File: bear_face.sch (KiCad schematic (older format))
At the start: 277 parts, among them J1 USB_B_Micro, J2 Conn_02x03_Odd_Even, Q1 2N7002, SW1 SW_Push, U1 ATmega32U4-AU, U2 SRV05-4, Y1 16MHz

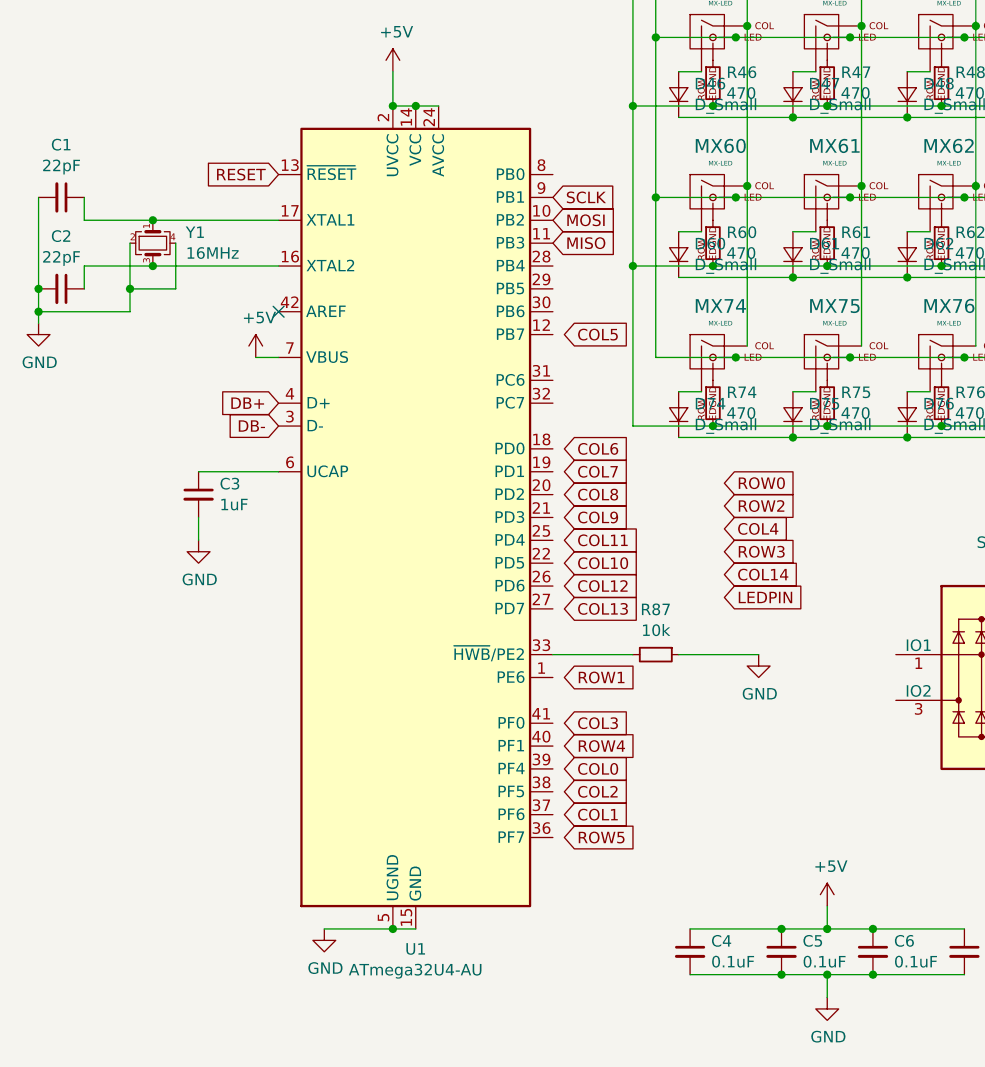
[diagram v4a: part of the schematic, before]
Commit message: +5V net tied in, matrix started
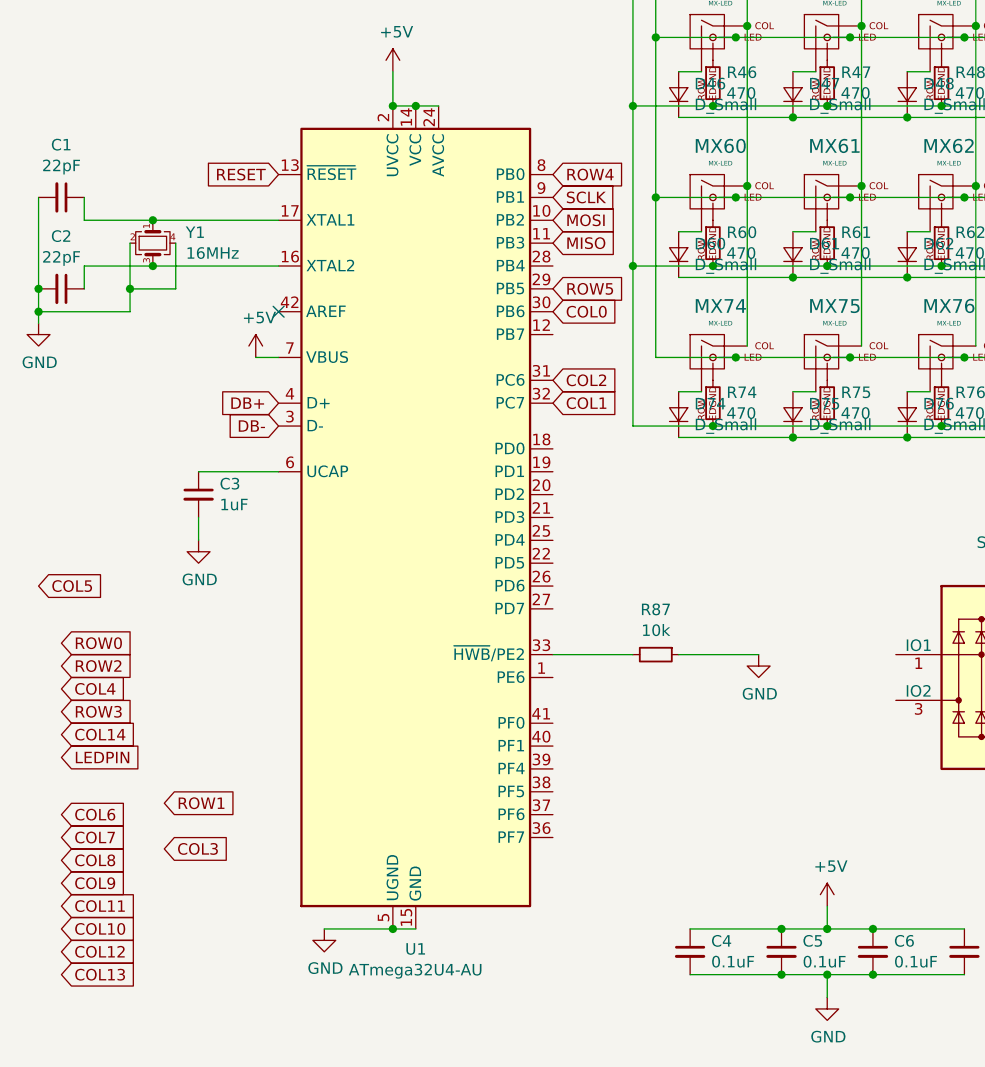
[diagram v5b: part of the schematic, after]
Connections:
- net COL0: now also U1.30 (PB6)
- net COL1: now also U1.32 (PC7)
- net COL2: now also U1.31 (PC6)
- net ROW4: now also U1.8 (PB0)
- net ROW5: now also U1.29 (PB5)
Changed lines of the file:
@@
 	1    0    0    -1
 $EndComp
-Text GLabel 3050 6700 2    50   Input ~ 0
+Text GLabel 3000 4300 2    50   Input ~ 0
 ROW5
-Text GLabel 3050 6200 2    50   Input ~ 0
+Text GLabel 1300 6750 2    50   Input ~ 0
 COL3
 NoConn ~ 1800 4400
-Text GLabel 3750 5150 2    50   Input ~ 0
+Text GLabel 850  5850 2    50   Input ~ 0
 ROW0
-Text GLabel 3050 6000 2    50   Input ~ 0
+Text GLabel 1300 6550 2    50   Input ~ 0
 ROW1
-Text GLabel 3750 5250 2    50   Input ~ 0
+Text GLabel 850  5950 2    50   Input ~ 0
 ROW2
-Text GLabel 3750 5450 2    50   Input ~ 0
+Text GLabel 850  6150 2    50   Input ~ 0
 ROW3
-Text GLabel 3050 4500 2    50   Input ~ 0
+Text GLabel 750  5600 2    50   Input ~ 0
 COL5
-Text GLabel 3050 5100 2    50   Input ~ 0
+Text GLabel 850  6700 2    50   Input ~ 0
 COL7
-Text GLabel 3050 5200 2    50   Input ~ 0
+Text GLabel 850  6800 2    50   Input ~ 0
 COL8
-Text GLabel 3050 5300 2    50   Input ~ 0
+Text GLabel 850  6900 2    50   Input ~ 0
 COL9
-Text GLabel 3050 5500 2    50   Input ~ 0
+Text GLabel 850  7100 2    50   Input ~ 0
 COL10
-Text GLabel 3050 5400 2    50   Input ~ 0
+Text GLabel 850  7000 2    50   Input ~ 0
 COL11
-Text GLabel 3050 5600 2    50   Input ~ 0
+Text GLabel 850  7200 2    50   Input ~ 0
 COL12
-Text GLabel 3050 5700 2    50   Input ~ 0
+Text GLabel 850  7300 2    50   Input ~ 0
 COL13
-Text GLabel 3750 5550 2    50   Input ~ 0
+Text GLabel 850  6250 2    50   Input ~ 0
 COL14
-Text GLabel 3750 5350 2    50   Input ~ 0
+Text GLabel 850  6050 2    50   Input ~ 0
 COL4
-Text GLabel 3050 5000 2    50   Input ~ 0
+Text GLabel 850  6600 2    50   Input ~ 0
 COL6
-Text GLabel 3050 6300 2    50   Input ~ 0
+Text GLabel 3000 3800 2    50   Input ~ 0
 ROW4
 Text GLabel 2650 2400 2    50   Input ~ 0
@@
 Wire Wire Line
 	1700 4600 1800 4600
-Text GLabel 3050 6500 2    50   Input ~ 0
+Text GLabel 3000 4700 2    50   Input ~ 0
 COL2
-Text GLabel 3050 6600 2    50   Input ~ 0
+Text GLabel 3000 4800 2    50   Input ~ 0
 COL1
-Text GLabel 3050 6400 2    50   Input ~ 0
+Text GLabel 3000 4400 2    50   Input ~ 0
 COL0
 NoConn ~ 1500 2600
-Text GLabel 3750 5650 2    50   Input ~ 0
+Text GLabel 850  6350 2    50   Input ~ 0
 LEDPIN
 Text GLabel 3350 1100 1    50   Input ~ 0

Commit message: Initial branch commit
LED only for Caps Lock, updated footprints
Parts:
- removed R10, R11, R12, R13, R14, R15, R16, R17, R18, R19, R2, R20, R21, R22, R23, R24, R25, R26, R27, R28, R29, R3, R30, R31, R32, R33, R34, R35, R36, R37, R38, R39, R4, R40, R41, R42, R43, R44, R45, R46, R47, R48, R49, R5, R50, R51, R52, R53, R54, R55, R56, R57, R58, R59, R6, R60, R61, R62, R63, R64, R65, R66, R67, R68, R69, R7, R70, R71, R72, R73, R74, R75, R76, R77, R78, R79, R8, R80, R81, R82, R83, R9: 470, Keebio-Parts:Resistor-Hybrid, symbol Device:R_Small
- MX1, MX15, MX31, MX44: value MX-LED -> MX-NoLED; footprint bear_face_parts:MXOnly-1.5U -> bear_face_parts:MXOnly-1.5U-NoLED; symbol MX_Alps_Hybrid:MX-LED -> MX_Alps_Hybrid:MX-NoLED
- MX10, MX11, MX12, MX13, MX14, MX16, MX17, MX18, MX19, MX20, MX21, MX22, MX23, MX24, MX25, MX26, MX27, MX28, MX3, MX30, MX32, MX33, MX34, MX35, MX36, MX37, MX38, MX39, MX4, MX40, MX41, MX42, MX43, MX45, MX47, MX48, MX49, MX5, MX50, MX51, MX52, MX53, MX54, MX55, MX56, MX57, MX59, MX6, MX61, MX62, MX63, MX64, MX65, MX66, MX67, MX68, MX69, MX7, MX70, MX72, MX73, MX78, MX79, MX8, MX80, MX81, MX82, MX83, MX9: value MX-LED -> MX-NoLED; footprint bear_face_parts:MXOnly-1U -> bear_face_parts:MXOnly-1U-NoLED; symbol MX_Alps_Hybrid:MX-LED -> MX_Alps_Hybrid:MX-NoLED
- MX2: value MX-LED -> MX_NoLED; footprint bear_face_parts:MXOnly-1U -> bear_face_parts:MXOnly-1U-NoLED; symbol MX_Alps_Hybrid:MX-LED -> MX_Alps_Hybrid:MX-NoLED
- MX29: value MX-LED -> MX-NoLED; footprint bear_face_parts:MXOnly-2U-NoStabs -> bear_face_parts:MXOnly-2U-NoLED-NoStabs; symbol MX_Alps_Hybrid:MX-LED -> MX_Alps_Hybrid:MX-NoLED
- MX46: value MX-LED -> MX-NoLED; footprint bear_face_parts:MXOnly-1.75U -> MX_Only:MXOnly-1.75U
- MX58, MX60: value MX-LED -> MX-NoLED; footprint bear_face_parts:MXOnly-2.25U-NoStabs -> bear_face_parts:MXOnly-2.25U-NoLED-NoStabs; symbol MX_Alps_Hybrid:MX-LED -> MX_Alps_Hybrid:MX-NoLED
- MX71: value MX-LED -> MX-NoLED; footprint bear_face_parts:MXOnly-1.75U -> bear_face_parts:MXOnly-1.75U-NoLED; symbol MX_Alps_Hybrid:MX-LED -> MX_Alps_Hybrid:MX-NoLED
- MX74, MX75, MX76: value MX-LED -> MX-NoLED; footprint bear_face_parts:MXOnly-1.25U -> bear_face_parts:MXOnly-1.25U-NoLED; symbol MX_Alps_Hybrid:MX-LED -> MX_Alps_Hybrid:MX-NoLED
- MX77: value MX-LED -> MX-NoLED; footprint bear_face_parts:MXOnly-6.25U-NoStabs -> bear_face_parts:MXOnly-6.25U-NoLED-NoStabs; symbol MX_Alps_Hybrid:MX-LED -> MX_Alps_Hybrid:MX-NoLED
- R1: value 470 -> R_Small; footprint Keebio-Parts:Resistor-Hybrid -> (none)
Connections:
- net +5V: no longer MX1.3 (LED), MX10.3 (LED), MX11.3 (LED), MX12.3 (LED), MX13.3 (LED), MX14.3 (LED), MX15.3 (LED), MX16.3 (LED), MX17.3 (LED), MX18.3 (LED), MX19.3 (LED), MX2.3 (LED), MX20.3 (LED), MX21.3 (LED), MX22.3 (LED), MX23.3 (LED), MX24.3 (LED), MX25.3 (LED), MX26.3 (LED), MX27.3 (LED), MX28.3 (LED), MX29.3 (LED), MX3.3 (LED), MX30.3 (LED), MX31.3 (LED), MX32.3 (LED), MX33.3 (LED), MX34.3 (LED), MX35.3 (LED), MX36.3 (LED), MX37.3 (LED), MX38.3 (LED), MX39.3 (LED), MX4.3 (LED), MX40.3 (LED), MX41.3 (LED), MX42.3 (LED), MX43.3 (LED), MX44.3 (LED), MX45.3 (LED), MX47.3 (LED), MX48.3 (LED), MX49.3 (LED), MX5.3 (LED), MX50.3 (LED), MX51.3 (LED), MX52.3 (LED), MX53.3 (LED), MX54.3 (LED), MX55.3 (LED), MX56.3 (LED), MX57.3 (LED), MX58.3 (LED), MX59.3 (LED), MX6.3 (LED), MX60.3 (LED), MX61.3 (LED), MX62.3 (LED), MX63.3 (LED), MX64.3 (LED), MX65.3 (LED), MX66.3 (LED), MX67.3 (LED), MX68.3 (LED), MX69.3 (LED), MX7.3 (LED), MX70.3 (LED), MX71.3 (LED), MX72.3 (LED), MX73.3 (LED), MX74.3 (LED), MX75.3 (LED), MX76.3 (LED), MX77.3 (LED), MX78.3 (LED), MX79.3 (LED), MX8.3 (LED), MX80.3 (LED), MX81.3 (LED), MX82.3 (LED), MX83.3 (LED), MX9.3 (LED)
- net at MX46.4 (LEDGND): now also R1.1

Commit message: Routing tweaks
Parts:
- R5: renamed from R1; footprint (none) -> Keebio-Parts:Resistor-Hybrid
- renumbered R85 to R1, R86 to R2, R87 to R3, R88 to R4
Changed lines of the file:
@@
 F 2 "Keebio-Parts:Diode-dual" V 3550 1350 50  0001 C CNN
 F 3 "~" V 3550 1350 50  0001 C CNN
+F 4 "" V 3550 1350 50  0001 C CNN "Cxxxxx"
 	1    3550 1350
 	0    -1   -1   0
@@
 $EndComp
 $Comp
-L Device:R_Small R85
+L Device:R_Small R1
 U 1 1 5E2BAE37
 P 1850 2400
-F 0 "R85" V 1654 2400 50  0000 C CNN
+F 0 "R1" V 1654 2400 50  0000 C CNN
 F 1 "22" V 1745 2400 50  0000 C CNN
 F 2 "Resistor_SMD:R_0805_2012Metric_Pad1.15x1.40mm_HandSolder" H 1850 2400 50  0001 C CNN
@@
 $EndComp
 $Comp
-L Device:R_Small R86
+L Device:R_Small R2
 U 1 1 5E2BDE9E
 P 2100 2500
-F 0 "R86" V 1904 2500 50  0000 C CNN
+F 0 "R2" V 1904 2500 50  0000 C CNN
 F 1 "22" V 1995 2500 50  0000 C CNN
 F 2 "Resistor_SMD:R_0805_2012Metric_Pad1.15x1.40mm_HandSolder" H 2100 2500 50  0001 C CNN
@@
 	8500 5550 8500 5650
 $Comp
-L Device:R_Small R87
+L Device:R_Small R3
 U 1 1 5E285AAF
 P 3450 5900
-F 0 "R87" V 3254 5900 50  0000 C CNN
+F 0 "R3" V 3254 5900 50  0000 C CNN
 F 1 "10k" V 3345 5900 50  0000 C CNN
 F 2 "Resistor_SMD:R_0805_2012Metric_Pad1.15x1.40mm_HandSolder" H 3450 5900 50  0001 C CNN
@@
 Connection ~ 5850 7000
 $Comp
-L Device:R_Small R88
+L Device:R_Small R4
 U 1 1 5E33D046
 P 5850 7100
-F 0 "R88" H 5909 7146 50  0000 L CNN
+F 0 "R4" H 5909 7146 50  0000 L CNN
 F 1 "4.7k" H 5909 7055 50  0000 L CNN
 F 2 "Keebio-Parts:Resistor-Hybrid" H 5850 7100 50  0001 C CNN
@@
 $EndComp
 $Comp
-L Device:R_Small R1
+L Device:R_Small R5
 U 1 1 5E6C94F1
 P 3700 3400
-F 0 "R1" H 3759 3446 50  0000 L CNN
+F 0 "R5" H 3759 3446 50  0000 L CNN
 F 1 "R_Small" H 3759 3355 50  0000 L CNN
-F 2 "" H 3700 3400 50  0001 C CNN
+F 2 "Keebio-Parts:Resistor-Hybrid" H 3700 3400 50  0001 C CNN
 F 3 "~" H 3700 3400 50  0001 C CNN
 	1    3700 3400

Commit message: Columns routed, MCU pins broken out
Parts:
- D1, D2: LCSC# (none) -> C81598
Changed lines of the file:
@@
 F 2 "Keebio-Parts:Diode-dual" V 3550 1350 50  0001 C CNN
 F 3 "~" V 3550 1350 50  0001 C CNN
-F 4 "" V 3550 1350 50  0001 C CNN "Cxxxxx"
+F 4 " C81598" V 3550 1350 50  0001 C CNN "LCSC#"
 	1    3550 1350
 	0    -1   -1   0
@@
 F 2 "Keebio-Parts:Diode-dual" V 4050 1350 50  0001 C CNN
 F 3 "~" V 4050 1350 50  0001 C CNN
+F 4 " C81598" V 4050 1350 50  0001 C CNN "LCSC#"
 	1    4050 1350
 	0    -1   -1   0
